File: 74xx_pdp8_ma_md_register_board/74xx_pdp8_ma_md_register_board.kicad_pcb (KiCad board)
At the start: 4 copper layers, 137.2 x 88.9 mm, 39 parts, among them P1 DIL24, P2 DIL24, P3 DIL24, P4 DIL24, P5 DIL24, U1 74HC125, U10 74HC04, U11 74HC163, U12 74HC163, U13 74HC163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

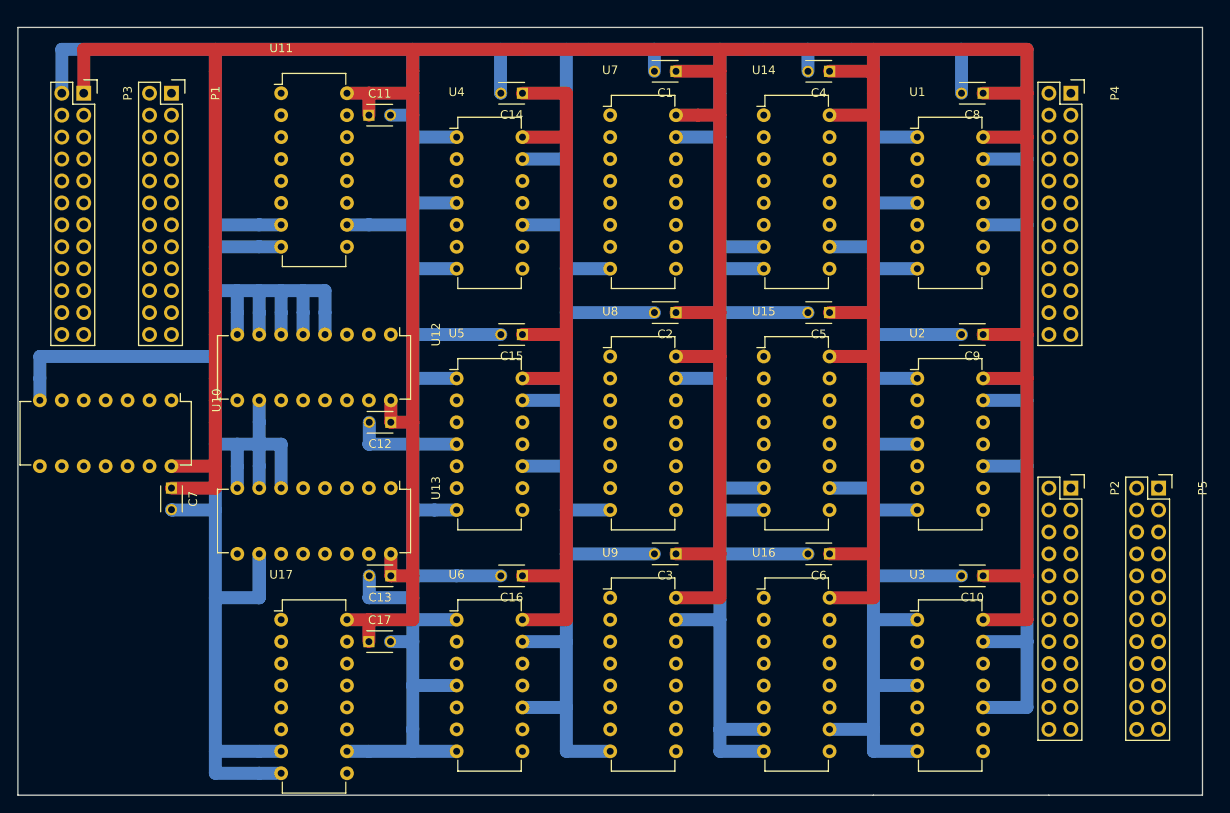
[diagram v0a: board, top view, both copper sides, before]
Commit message: Big changes - elected to switch to board interconnections along one long edge only. Boards to connect to backplane via right-angled DIL connectors. Both register boards and register mux boards thusly modified.
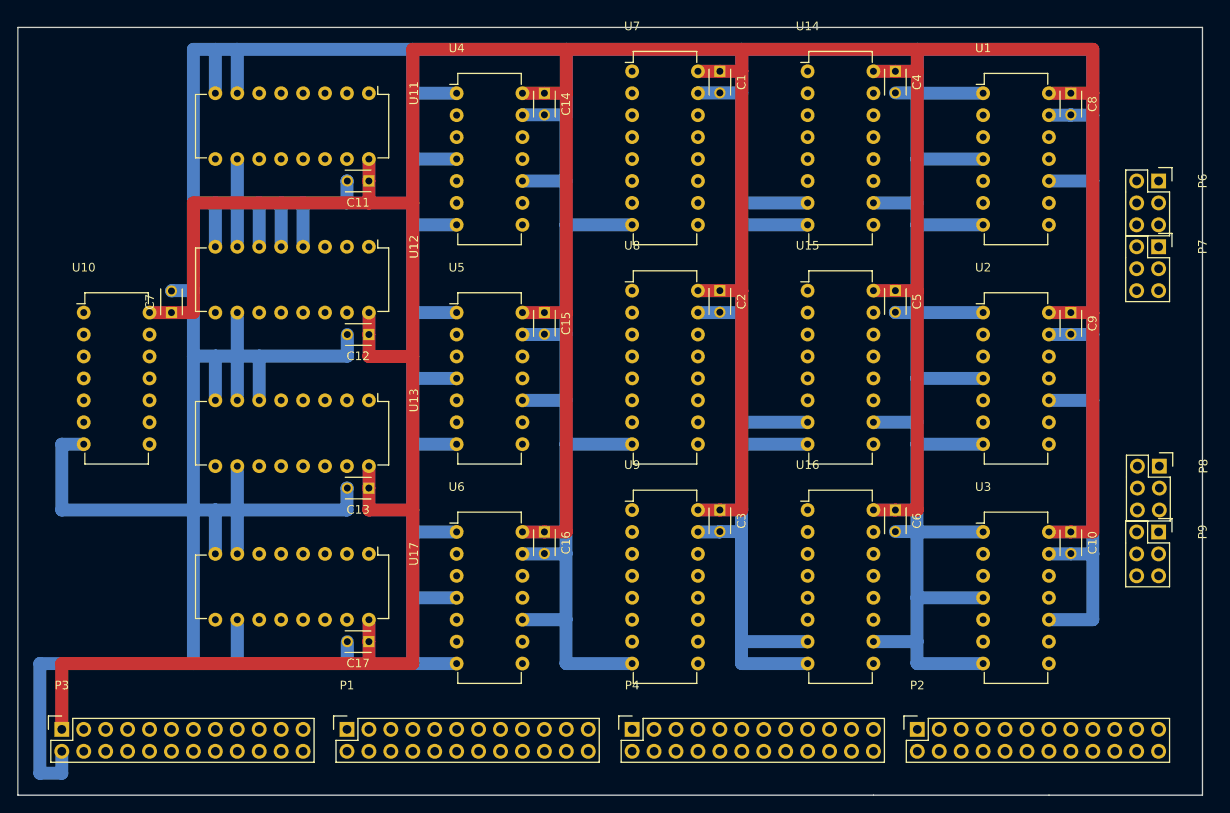
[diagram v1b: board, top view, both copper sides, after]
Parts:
- removed P5: DIL24, Socket_Strips:Socket_Strip_Straight_2x12
- added P6: DIL6, Socket_Strips:Socket_Strip_Straight_2x03, F.Cu at (149.9, 121.9)
- added P7: DIL6, Socket_Strips:Socket_Strip_Straight_2x03, F.Cu at (149.9, 129.5)
- added P8: DIL6, Socket_Strips:Socket_Strip_Straight_2x03, F.Cu at (149.9, 154.9)
- added P9: DIL6, Socket_Strips:Socket_Strip_Straight_2x03, F.Cu at (149.9, 162.6)
- moved P4 89.5 mm to (88.9, 185.4), turned to 0 degrees
- moved P1 76.4 mm to (55.9, 185.4), turned to 0 degrees
- moved P3 73.7 mm to (22.9, 185.4), turned to 0 degrees
- moved P2 33.1 mm to (121.9, 185.4), turned to 0 degrees
- moved C7 20.3 mm to (35.6, 137.2), turned to 90 degrees
- moved U10 14.4 mm to (25.4, 137.2), turned to 0 degrees
- moved U17 12.7 mm to (58.4, 165.1), turned to 270 degrees
- moved U3 12.7 mm to (129.5, 162.6)
- moved U16 11.4 mm to (109.2, 160.0)
- moved C10 11.4 mm to (139.7, 162.6), turned to 270 degrees
- moved U2 10.8 mm to (129.5, 137.2)
- moved C12 10.5 mm to (58.4, 139.7)
- moved U9 10.5 mm to (88.9, 160.0)
- moved C13 10.5 mm to (58.4, 157.5)
- moved U12 10.5 mm to (58.4, 129.5)
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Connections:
- U1 pad 11: (no net) -> /OUT_BUF_MA_3
- U1 pad 3: (no net) -> /OUT_BUF_MA_0
- U1 pad 6: (no net) -> /OUT_BUF_MA_1
- U1 pad 8: (no net) -> /OUT_BUF_MA_2
- U2 pad 11: (no net) -> /OUT_BUF_MA_7
- U2 pad 3: (no net) -> /OUT_BUF_MA_4
- U2 pad 6: (no net) -> /OUT_BUF_MA_5
- U2 pad 8: (no net) -> /OUT_BUF_MA_6
- U3 pad 11: (no net) -> /OUT_BUF_MA_11
- U3 pad 3: (no net) -> /OUT_BUF_MA_8
- U3 pad 6: (no net) -> /OUT_BUF_MA_9
- U3 pad 8: (no net) -> /OUT_BUF_MA_10
- U4 pad 11: (no net) -> /OUT_BUF_MD_3
- U4 pad 3: (no net) -> /OUT_BUF_MD_0
- U4 pad 6: (no net) -> /OUT_BUF_MD_1
- U4 pad 8: (no net) -> /OUT_BUF_MD_2
- U5 pad 11: (no net) -> /OUT_BUF_MD_7
- U5 pad 3: (no net) -> /OUT_BUF_MD_4
- U5 pad 6: (no net) -> /OUT_BUF_MD_5
- U5 pad 8: (no net) -> /OUT_BUF_MD_6
- U6 pad 11: (no net) -> /OUT_BUF_MD_11
- U6 pad 3: (no net) -> /OUT_BUF_MD_8
- U6 pad 6: (no net) -> /OUT_BUF_MD_9
- U6 pad 8: (no net) -> /OUT_BUF_MD_10
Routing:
- net (no net): track 121.9 -> 0.00 mm
- net VCC: track 647.7 -> 551.2 mm
- net GND: track 1105.5 -> 1035.4 mm
- net /OUT_BUF_MD_9: track 0.00 -> 5.16 mm
- net /OUT_BUF_MD_11: track 0.00 -> 5.16 mm
- net /OUT_BUF_MD_1: track 0.00 -> 5.16 mm
- net /OUT_BUF_MD_8: track 0.00 -> 5.08 mm
- net /OUT_BUF_MD_7: track 0.00 -> 5.08 mm
- net /OUT_BUF_MD_6: track 0.00 -> 5.08 mm
- net /OUT_BUF_MD_5: track 0.00 -> 5.08 mm
- net /OUT_BUF_MD_4: track 0.00 -> 5.08 mm
- net /OUT_BUF_MD_3: track 0.00 -> 5.08 mm
- net /OUT_BUF_MA_9: track 0.00 -> 5.08 mm
- net /OUT_BUF_MA_8: track 0.00 -> 5.08 mm
- net /OUT_BUF_MA_7: track 0.00 -> 5.08 mm
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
